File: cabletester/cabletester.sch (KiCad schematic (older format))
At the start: 25 parts, among them J1 Conn, J2 Conn, J3 Conn, J4 Conn, J5 OLED, U1 4051

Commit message: First version after fork, schematic cleanup and PCB
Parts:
- A1: footprint Module:Arduino_Nano -> ao_tht:Arduino_Nano; symbol cabletester-rescue:Arduino_Nano_v3.x-MCU_Module -> MCU_Module:Arduino_Nano_v3.x
- C1: footprint (none) -> ao_tht:C_Disc_D3.0mm_W1.6mm_P2.50mm
- J1, J3: value Conn -> IDC 2x5; footprint (none) -> ao_tht:Power_Header
- J2, J4: value Conn -> IDC 2x8; footprint (none) -> Connector_IDC:IDC-Header_2x08_P2.54mm_Vertical
- J5: footprint (none) -> Connector_PinSocket_2.54mm:PinSocket_1x04_P2.54mm_Vertical
- R1, R10, R11, R12, R13, R14, R15, R16, R17, R2, R3, R4, R5, R6, R7, R8, R9: footprint (none) -> ao_tht:R_Axial_DIN0207_L6.3mm_D2.5mm_P7.62mm_Horizontal
- U1: footprint (none) -> ao_tht:DIP-16_W7.62mm_Socket_LongPads
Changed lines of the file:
@@
 P 8900 4550
 F 0 "J4" H 8950 5067 50  0000 C CNN
-F 1 "Conn" H 8950 4976 50  0000 C CNN
-F 2 "" H 8900 4550 50  0001 C CNN
+F 1 "IDC 2x8" H 8950 4976 50  0000 C CNN
+F 2 "Connector_IDC:IDC-Header_2x08_P2.54mm_Vertical" H 8900 4550 50  0001 C CNN
 F 3 "~" H 8900 4550 50  0001 C CNN
 	1    8900 4550
@@
 P 5600 2650
 F 0 "J2" H 5650 3167 50  0000 C CNN
-F 1 "Conn" H 5650 3076 50  0000 C CNN
-F 2 "" H 5600 2650 50  0001 C CNN
+F 1 "IDC 2x8" H 5650 3076 50  0000 C CNN
+F 2 "Connector_IDC:IDC-Header_2x08_P2.54mm_Vertical" H 5600 2650 50  0001 C CNN
 F 3 "~" H 5600 2650 50  0001 C CNN
 	1    5600 2650
@@
 P 9800 4450
 F 0 "J3" H 9850 4867 50  0000 C CNN
-F 1 "Conn" H 9850 4776 50  0000 C CNN
-F 2 "" H 9800 4450 50  0001 C CNN
+F 1 "IDC 2x5" H 9850 4776 50  0000 C CNN
+F 2 "ao_tht:Power_Header" H 9800 4450 50  0001 C CNN
 F 3 "~" H 9800 4450 50  0001 C CNN
 	1    9800 4450
@@
 P 4700 2550
 F 0 "J1" H 4750 2967 50  0000 C CNN
-F 1 "Conn" H 4750 2876 50  0000 C CNN
-F 2 "" H 4700 2550 50  0001 C CNN
+F 1 "IDC 2x5" H 4750 2876 50  0000 C CNN
+F 2 "ao_tht:Power_Header" H 4700 2550 50  0001 C CNN
 F 3 "~" H 4700 2550 50  0001 C CNN
 	1    4700 2550
@@
 Connection ~ 5900 3050
 $Comp
-L cabletester-rescue:Arduino_Nano_v3.x-MCU_Module A1
+L MCU_Module:Arduino_Nano_v3.x A1
 U 1 1 5DF0BB02
 P 2300 4400
 F 0 "A1" H 2300 3100 50  0000 C CNN
 F 1 "Arduino_Nano_v3.x" H 2300 3000 50  0000 C CNN
-F 2 "Module:Arduino_Nano" H 2450 3450 50  0001 L CNN
+F 2 "ao_tht:Arduino_Nano" H 2450 3450 50  0001 L CNN
 F 3 "http://www.mouser.com/pdfdocs/Gravitech_Arduino_Nano3_0.pdf" H 2300 3400 50  0001 C CNN
 	1    2300 4400
@@
 F 0 "U1" H 5291 4304 50  0000 L CNN
 F 1 "4051" H 5291 4395 50  0000 L CNN
-F 2 "" H 4750 4350 50  0001 C CNN
+F 2 "ao_tht:DIP-16_W7.62mm_Socket_LongPads" H 4750 4350 50  0001 C CNN
 F 3 "http://www.intersil.com/content/dam/Intersil/documents/cd40/cd4051bms-52bms-53bms.pdf" H 4750 4350 50  0001 C CNN
 	1    4750 4350
@@
 F 0 "R10" H 5370 5796 50  0000 L CNN
 F 1 "10K" H 5370 5705 50  0000 L CNN
-F 2 "" V 5230 5750 50  0001 C CNN
+F 2 "ao_tht:R_Axial_DIN0207_L6.3mm_D2.5mm_P7.62mm_Horizontal" V 5230 5750 50  0001 C CNN
 F 3 "~" H 5300 5750 50  0001 C CNN
 	1    5300 5750
@@
 F 0 "R11" H 5670 5796 50  0000 L CNN
 F 1 "10K" H 5670 5705 50  0000 L CNN
-F 2 "" V 5530 5750 50  0001 C CNN
+F 2 "ao_tht:R_Axial_DIN0207_L6.3mm_D2.5mm_P7.62mm_Horizontal" V 5530 5750 50  0001 C CNN
 F 3 "~" H 5600 5750 50  0001 C CNN
 	1    5600 5750
@@
 F 0 "R12" H 5970 5796 50  0000 L CNN
 F 1 "10K" H 5970 5705 50  0000 L CNN
-F 2 "" V 5830 5750 50  0001 C CNN
+F 2 "ao_tht:R_Axial_DIN0207_L6.3mm_D2.5mm_P7.62mm_Horizontal" V 5830 5750 50  0001 C CNN
 F 3 "~" H 5900 5750 50  0001 C CNN
 	1    5900 5750
@@
 F 0 "R13" H 6270 5796 50  0000 L CNN
 F 1 "10K" H 6270 5705 50  0000 L CNN
-F 2 "" V 6130 5750 50  0001 C CNN
+F 2 "ao_tht:R_Axial_DIN0207_L6.3mm_D2.5mm_P7.62mm_Horizontal" V 6130 5750 50  0001 C CNN
 F 3 "~" H 6200 5750 50  0001 C CNN
 	1    6200 5750
@@
 F 0 "R14" H 6570 5796 50  0000 L CNN
 F 1 "10K" H 6570 5705 50  0000 L CNN
-F 2 "" V 6430 5750 50  0001 C CNN
+F 2 "ao_tht:R_Axial_DIN0207_L6.3mm_D2.5mm_P7.62mm_Horizontal" V 6430 5750 50  0001 C CNN
 F 3 "~" H 6500 5750 50  0001 C CNN
 	1    6500 5750
@@
 F 0 "R15" H 6870 5796 50  0000 L CNN
 F 1 "10K" H 6870 5705 50  0000 L CNN
-F 2 "" V 6730 5750 50  0001 C CNN
+F 2 "ao_tht:R_Axial_DIN0207_L6.3mm_D2.5mm_P7.62mm_Horizontal" V 6730 5750 50  0001 C CNN
 F 3 "~" H 6800 5750 50  0001 C CNN
 	1    6800 5750
@@
 F 0 "R16" H 7170 5796 50  0000 L CNN
 F 1 "10K" H 7170 5705 50  0000 L CNN
-F 2 "" V 7030 5750 50  0001 C CNN
+F 2 "ao_tht:R_Axial_DIN0207_L6.3mm_D2.5mm_P7.62mm_Horizontal" V 7030 5750 50  0001 C CNN
 F 3 "~" H 7100 5750 50  0001 C CNN
 	1    7100 5750
@@
 F 0 "R17" H 7470 5796 50  0000 L CNN
 F 1 "10K" H 7470 5705 50  0000 L CNN
-F 2 "" V 7330 5750 50  0001 C CNN
+F 2 "ao_tht:R_Axial_DIN0207_L6.3mm_D2.5mm_P7.62mm_Horizontal" V 7330 5750 50  0001 C CNN
 F 3 "~" H 7400 5750 50  0001 C CNN
 	1    7400 5750
@@
 F 0 "R1" H 6080 2154 50  0000 R CNN
 F 1 "1K" H 6080 2245 50  0000 R CNN
-F 2 "" V 6080 2200 50  0001 C CNN
+F 2 "ao_tht:R_Axial_DIN0207_L6.3mm_D2.5mm_P7.62mm_Horizontal" V 6080 2200 50  0001 C CNN
 F 3 "~" H 6150 2200 50  0001 C CNN
 	1    6150 2200
@@
 F 0 "R2" H 6380 2254 50  0000 R CNN
 F 1 "1K" H 6380 2345 50  0000 R CNN
-F 2 "" V 6380 2300 50  0001 C CNN
+F 2 "ao_tht:R_Axial_DIN0207_L6.3mm_D2.5mm_P7.62mm_Horizontal" V 6380 2300 50  0001 C CNN
 F 3 "~" H 6450 2300 50  0001 C CNN
 	1    6450 2300
@@
 F 0 "R3" H 6680 2354 50  0000 R CNN
 F 1 "1K" H 6680 2445 50  0000 R CNN
-F 2 "" V 6680 2400 50  0001 C CNN
+F 2 "ao_tht:R_Axial_DIN0207_L6.3mm_D2.5mm_P7.62mm_Horizontal" V 6680 2400 50  0001 C CNN
 F 3 "~" H 6750 2400 50  0001 C CNN
 	1    6750 2400
@@
 F 0 "R4" H 6980 2454 50  0000 R CNN
 F 1 "1K" H 6980 2545 50  0000 R CNN
-F 2 "" V 6980 2500 50  0001 C CNN
+F 2 "ao_tht:R_Axial_DIN0207_L6.3mm_D2.5mm_P7.62mm_Horizontal" V 6980 2500 50  0001 C CNN
 F 3 "~" H 7050 2500 50  0001 C CNN
 	1    7050 2500
@@
 F 0 "R5" H 7280 2554 50  0000 R CNN
 F 1 "1K" H 7280 2645 50  0000 R CNN
-F 2 "" V 7280 2600 50  0001 C CNN
+F 2 "ao_tht:R_Axial_DIN0207_L6.3mm_D2.5mm_P7.62mm_Horizontal" V 7280 2600 50  0001 C CNN
 F 3 "~" H 7350 2600 50  0001 C CNN
 	1    7350 2600
@@
 F 0 "R6" H 7580 2654 50  0000 R CNN
 F 1 "1K" H 7580 2745 50  0000 R CNN
-F 2 "" V 7580 2700 50  0001 C CNN
+F 2 "ao_tht:R_Axial_DIN0207_L6.3mm_D2.5mm_P7.62mm_Horizontal" V 7580 2700 50  0001 C CNN
 F 3 "~" H 7650 2700 50  0001 C CNN
 	1    7650 2700
@@
 F 0 "R7" H 7880 2754 50  0000 R CNN
 F 1 "1K" H 7880 2845 50  0000 R CNN
-F 2 "" V 7880 2800 50  0001 C CNN
+F 2 "ao_tht:R_Axial_DIN0207_L6.3mm_D2.5mm_P7.62mm_Horizontal" V 7880 2800 50  0001 C CNN
 F 3 "~" H 7950 2800 50  0001 C CNN
 	1    7950 2800
@@
 F 0 "R8" H 8180 2854 50  0000 R CNN
 F 1 "1K" H 8180 2945 50  0000 R CNN
-F 2 "" V 8180 2900 50  0001 C CNN
+F 2 "ao_tht:R_Axial_DIN0207_L6.3mm_D2.5mm_P7.62mm_Horizontal" V 8180 2900 50  0001 C CNN
 F 3 "~" H 8250 2900 50  0001 C CNN
 	1    8250 2900
@@
 F 0 "R9" H 8480 2954 50  0000 R CNN
 F 1 "1K" H 8480 3045 50  0000 R CNN
-F 2 "" V 8480 3000 50  0001 C CNN
+F 2 "ao_tht:R_Axial_DIN0207_L6.3mm_D2.5mm_P7.62mm_Horizontal" V 8480 3000 50  0001 C CNN
 F 3 "~" H 8550 3000 50  0001 C CNN
 	1    8550 3000
@@
 F 0 "C1" H 4365 5596 50  0000 L CNN
 F 1 "100n" H 4365 5505 50  0000 L CNN
-F 2 "" H 4288 5400 50  0001 C CNN
+F 2 "ao_tht:C_Disc_D3.0mm_W1.6mm_P2.50mm" H 4288 5400 50  0001 C CNN
 F 3 "~" H 4250 5550 50  0001 C CNN
 	1    4250 5550
@@
 F 0 "J5" H 3100 5200 50  0000 L CNN
 F 1 "OLED" H 3050 5300 50  0000 L CNN
-F 2 "" H 3150 5600 50  0001 C CNN
+F 2 "Connector_PinSocket_2.54mm:PinSocket_1x04_P2.54mm_Vertical" H 3150 5600 50  0001 C CNN
 F 3 "~" H 3150 5600 50  0001 C CNN
 	1    3150 5600

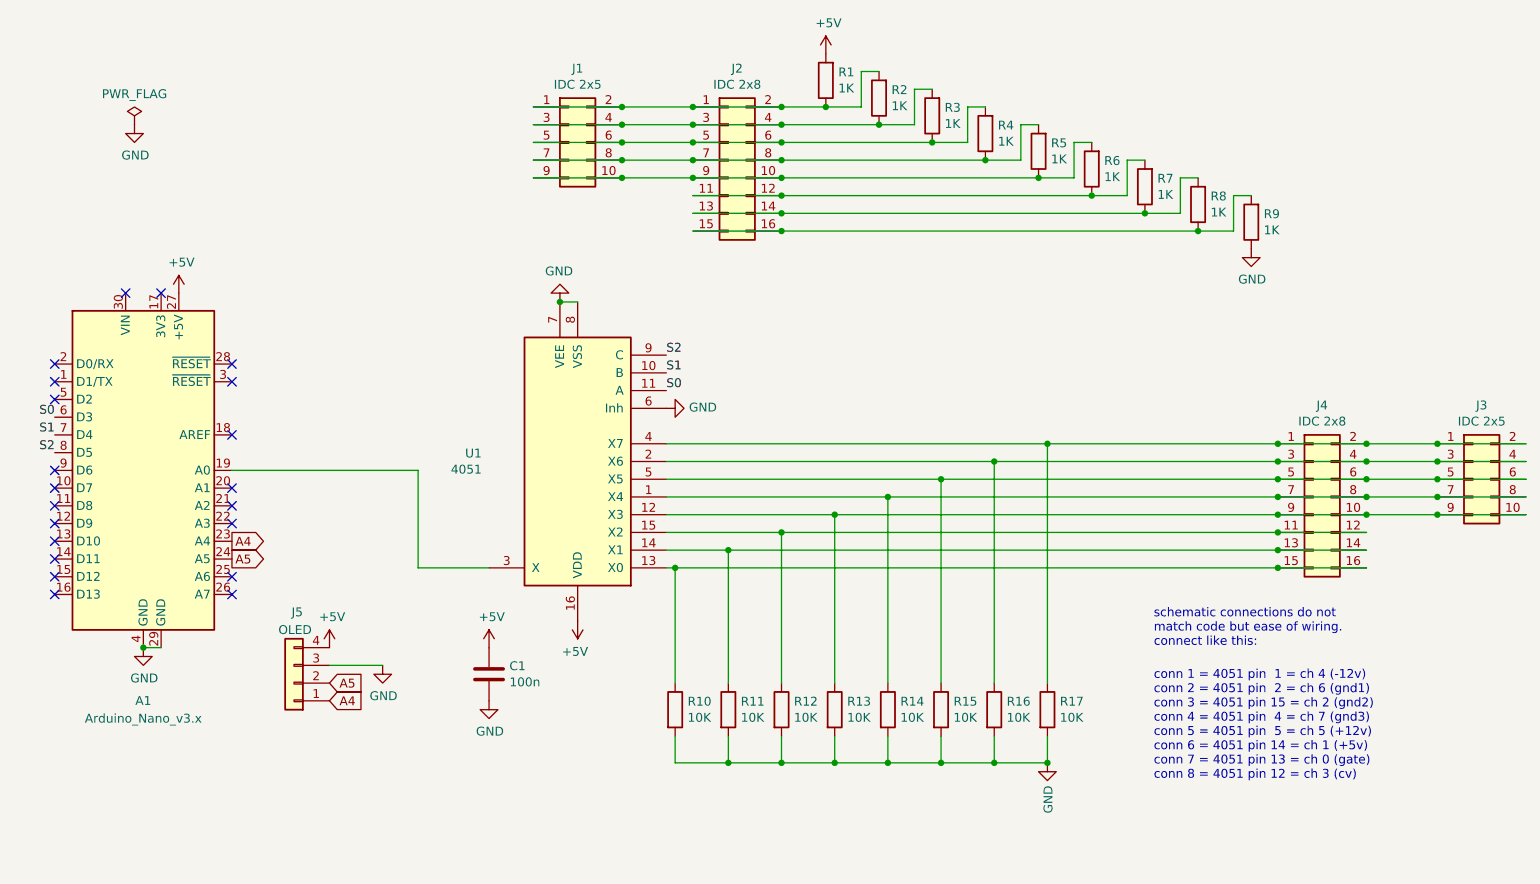
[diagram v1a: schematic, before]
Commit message: labels to globals, page settings
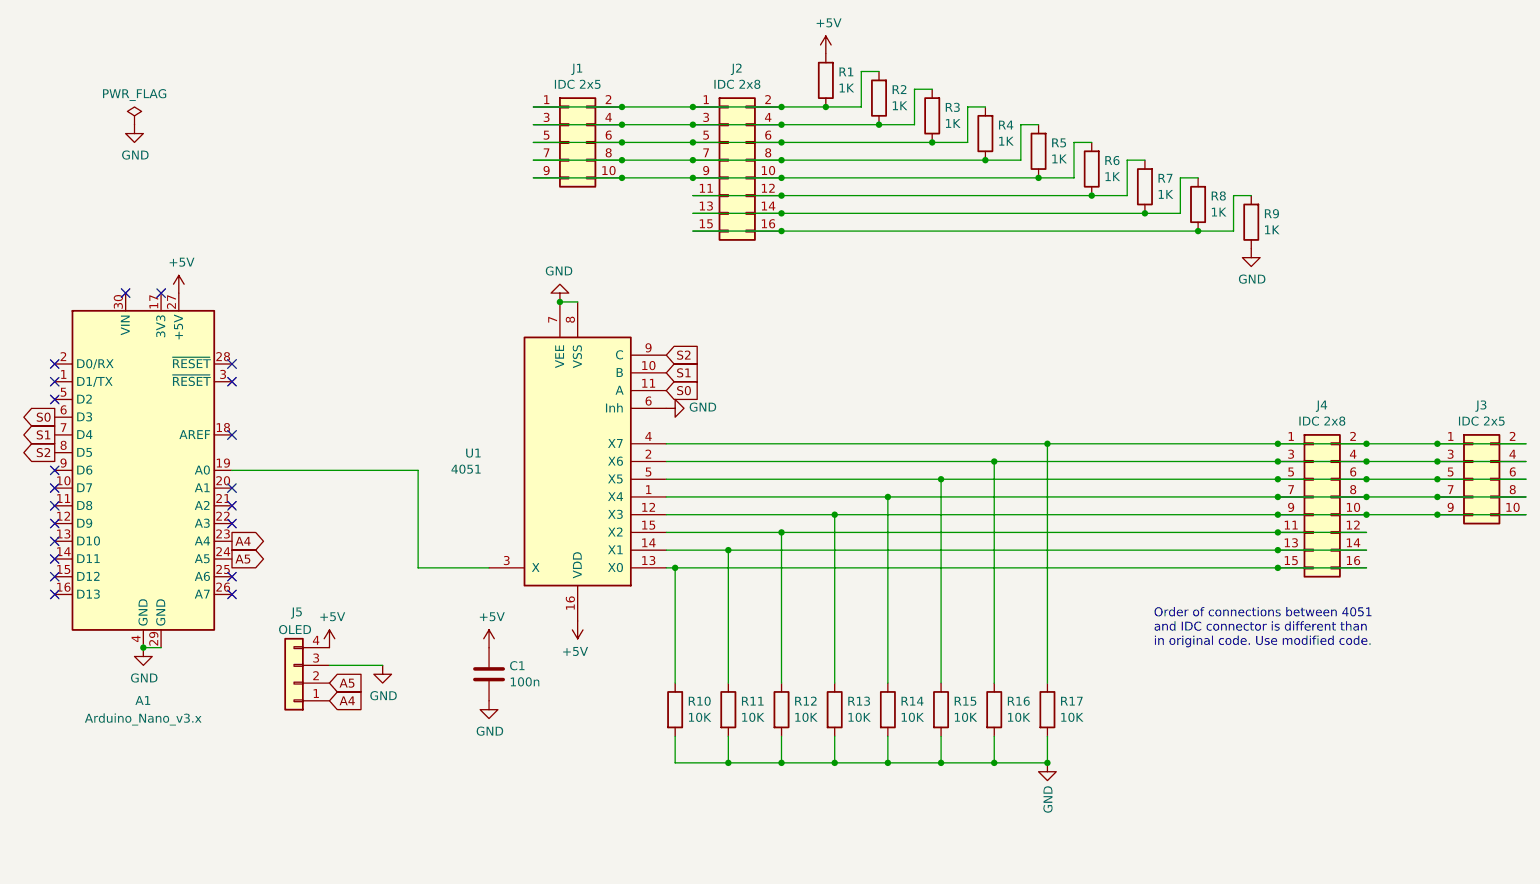
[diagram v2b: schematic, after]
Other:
- note added: "Order of connections between 4051\nand IDC connector is different than\nin original code. Use modified code."
- note removed: "conn 1 = 4051 pin 1 = ch 4 (-12v)\nconn 2 = 4051 pin 2 = ch 6 (gnd1)\nconn 3 = 4051 pin 15 = ch 2 (gnd2)\nconn 4 = 4051 pin 4 = ch 7 (gnd3)\nconn 5 = 4051 pin 5 = ch 5 (+12v)\nconn 6 = 4051 pin 14 = ch 1 (+5v)\nconn 7 = 4051 pin 13 = ch 0 (gate)\nconn 8 = 4051 pin 12 = ch 3 (cv)"
- note removed: "schematic connections do not \nmatch code but ease of wiring.\nconnect like this:"
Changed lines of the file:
@@
 Date ""
 Rev ""
-Comp ""
-Comment1 ""
+Comp "tomarus / https://github.com/tomarus/cabletester"
+Comment1 "forked to https://github.com/holmesrichards/cabletester with slight mods"
 Comment2 ""
 Comment3 ""
@@
 Connection ~ 5900 2950
 Connection ~ 5900 3050
-$Comp
-L MCU_Module:Arduino_Nano_v3.x A1
-U 1 1 5DF0BB02
-P 2300 4400
-F 0 "A1" H 2300 3100 50  0000 C CNN
-F 1 "Arduino_Nano_v3.x" H 2300 3000 50  0000 C CNN
-F 2 "ao_tht:Arduino_Nano" H 2450 3450 50  0001 L CNN
-F 3 "http://www.mouser.com/pdfdocs/Gravitech_Arduino_Nano3_0.pdf" H 2300 3400 50  0001 C CNN
-	1    2300 4400
-	1    0    0    -1
-$EndComp
 $Comp
 L power:GND #PWR011
@@
 Wire Wire Line
 	3850 4950 4250 4950
-Text Label 5250 3950 0    50   ~ 0
-S0
-Text Label 5250 3850 0    50   ~ 0
-S1
-Text Label 5250 3750 0    50   ~ 0
-S2
-Text Label 1800 4100 2    50   ~ 0
-S0
-Text Label 1800 4200 2    50   ~ 0
-S1
-Text Label 1800 4300 2    50   ~ 0
-S2
 NoConn ~ 1800 4400
 NoConn ~ 1800 4500
@@
 	1    0    0    -1
 $EndComp
-NoConn ~ 1800 4000
 NoConn ~ 1800 3900
 NoConn ~ 1800 3800
@@
 $EndComp
 Text Notes 8000 5400 0    50   ~ 0
-schematic connections do not \nmatch code but ease of wiring.\nconnect like this:
+Order of connections between 4051\nand IDC connector is different than\nin original code. Use modified code.
 Wire Wire Line
 	5300 4950 5300 5600
@@
 	1    0    0    -1
 $EndComp
-Text Notes 8000 6150 0    50   ~ 0
-conn 1 = 4051 pin  1 = ch 4 (-12v)\nconn 2 = 4051 pin  2 = ch 6 (gnd1)\nconn 3 = 4051 pin 15 = ch 2 (gnd2)\nconn 4 = 4051 pin  4 = ch 7 (gnd3)\nconn 5 = 4051 pin  5 = ch 5 (+12v)\nconn 6 = 4051 pin 14 = ch 1 (+5v)\nconn 7 = 4051 pin 13 = ch 0 (gate)\nconn 8 = 4051 pin 12 = ch 3 (cv)
 Connection ~ 6450 2450
 Wire Wire Line
@@
 	4750 3450 4650 3450
 Connection ~ 4650 3450
+NoConn ~ 1800 4000
+$Comp
+L MCU_Module:Arduino_Nano_v3.x A1
+U 1 1 5DF0BB02
+P 2300 4400
+F 0 "A1" H 2300 3100 50  0000 C CNN
+F 1 "Arduino_Nano_v3.x" H 2300 3000 50  0000 C CNN
+F 2 "ao_tht:Arduino_Nano" H 2450 3450 50  0001 L CNN
+F 3 "http://www.mouser.com/pdfdocs/Gravitech_Arduino_Nano3_0.pdf" H 2300 3400 50  0001 C CNN
+	1    2300 4400
+	1    0    0    -1
+$EndComp
+Text GLabel 1800 4100 0    50   Output ~ 0
+S0
+Text GLabel 1800 4200 0    50   Output ~ 0
+S1
+Text GLabel 1800 4300 0    50   Output ~ 0
+S2
+Text GLabel 5250 3950 2    50   Input ~ 0
+S0
+Text GLabel 5250 3850 2    50   Input ~ 0
+S1
+Text GLabel 5250 3750 2    50   Input ~ 0
+S2
 $EndSCHEMATC

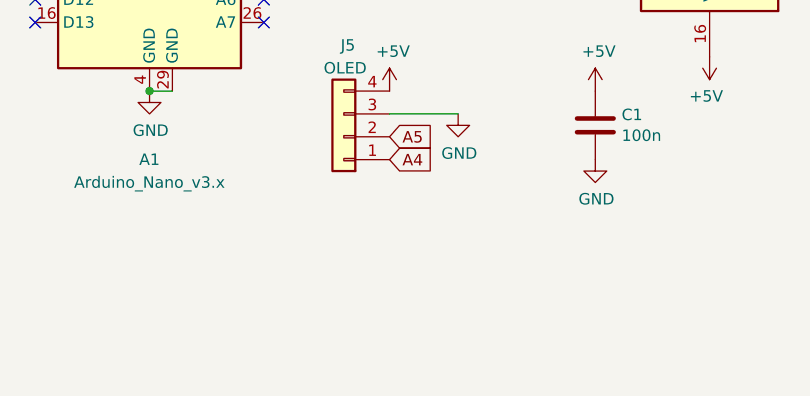
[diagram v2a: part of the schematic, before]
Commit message: Add 2nd header for alternate OLED pinout
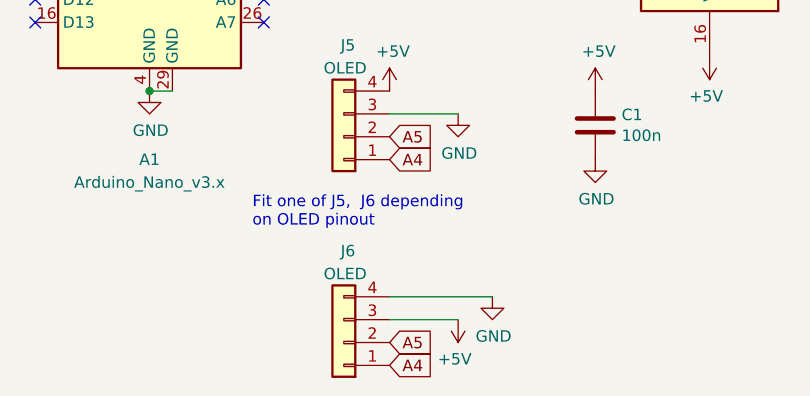
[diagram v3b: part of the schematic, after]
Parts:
- added J6: OLED, Connector_PinSocket_2.54mm:PinSocket_1x04_P2.54mm_Vertical, symbol Connector_Generic:Conn_01x04
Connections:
- net +5V: now also J6.3 (Pin_3)
- net A4: now also J6.1 (Pin_1)
- net A5: now also J6.2 (Pin_2)
- net GND: now also J6.4 (Pin_4)
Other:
- note added: "Fit one of J5, J6 depending\non OLED pinout"
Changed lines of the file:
@@
 Text GLabel 5250 3750 2    50   Input ~ 0
 S2
+$Comp
+L power:GND #PWR06
+U 1 1 5F324521
+P 3800 6300
+F 0 "#PWR06" H 3800 6050 50  0001 C CNN
+F 1 "GND" H 3805 6127 50  0000 C CNN
+F 2 "" H 3800 6300 50  0001 C CNN
+F 3 "" H 3800 6300 50  0001 C CNN
+	1    3800 6300
+	1    0    0    -1
+$EndComp
+Text GLabel 3350 6600 2    50   Input ~ 0
+A4
+Text GLabel 3350 6500 2    50   Input ~ 0
+A5
+$Comp
+L Connector_Generic:Conn_01x04 J6
+U 1 1 5F324527
+P 3150 6500
+F 0 "J6" H 3100 6100 50  0000 L CNN
+F 1 "OLED" H 3050 6200 50  0000 L CNN
+F 2 "Connector_PinSocket_2.54mm:PinSocket_1x04_P2.54mm_Vertical" H 3150 6500 50  0001 C CNN
+F 3 "~" H 3150 6500 50  0001 C CNN
+	1    3150 6500
+	-1   0    0    1
+$EndComp
+$Comp
+L power:+5V #PWR012
+U 1 1 5F32451B
+P 3650 6400
+F 0 "#PWR012" H 3650 6250 50  0001 C CNN
+F 1 "+5V" H 3665 6573 50  0000 C CNN
+F 2 "" H 3650 6400 50  0001 C CNN
+F 3 "" H 3650 6400 50  0001 C CNN
+	1    3650 6400
+	-1   0    0    1
+$EndComp
+Wire Wire Line
+	3350 6400 3650 6400
+Wire Wire Line
+	3350 6300 3800 6300
+Text Notes 2750 6000 0    50   ~ 0
+Fit one of J5,  J6 depending\non OLED pinout
 $EndSCHEMATC

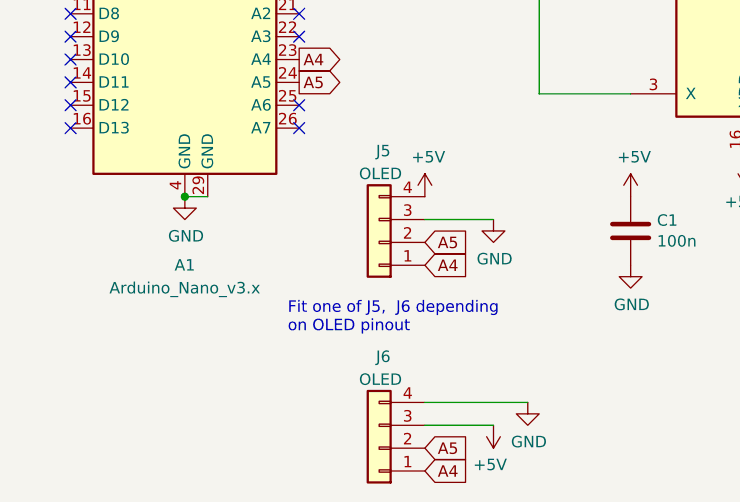
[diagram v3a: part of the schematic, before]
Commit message: BOM; change header label
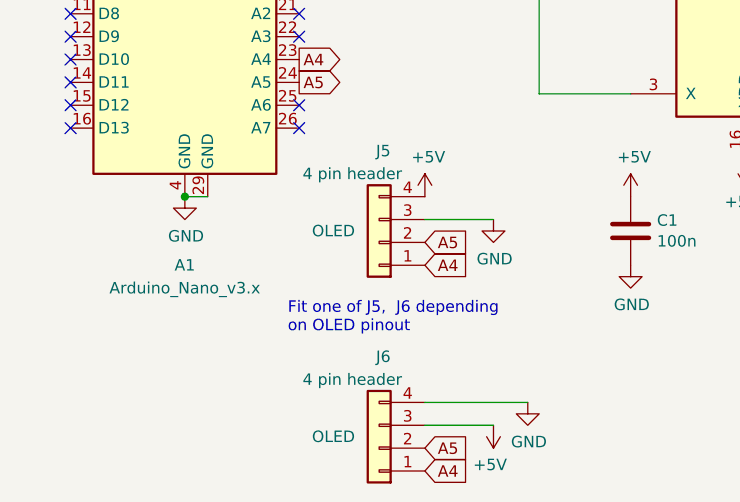
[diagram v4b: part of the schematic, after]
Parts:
- J5, J6: value OLED -> 4 pin header; Field4 (none) -> OLED
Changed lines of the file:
@@
 P 3150 5600
 F 0 "J5" H 3100 5200 50  0000 L CNN
-F 1 "OLED" H 3050 5300 50  0000 L CNN
+F 1 "4 pin header" H 3050 5300 50  0000 L CNN
 F 2 "Connector_PinSocket_2.54mm:PinSocket_1x04_P2.54mm_Vertical" H 3150 5600 50  0001 C CNN
 F 3 "~" H 3150 5600 50  0001 C CNN
+F 4 "OLED" H 3350 5550 50  0000 C CNN "Field4"
 	1    3150 5600
 	-1   0    0    1
@@
 P 3150 6500
 F 0 "J6" H 3100 6100 50  0000 L CNN
-F 1 "OLED" H 3050 6200 50  0000 L CNN
+F 1 "4 pin header" H 3050 6200 50  0000 L CNN
 F 2 "Connector_PinSocket_2.54mm:PinSocket_1x04_P2.54mm_Vertical" H 3150 6500 50  0001 C CNN
 F 3 "~" H 3150 6500 50  0001 C CNN
+F 4 "OLED" H 3350 6450 50  0000 C CNN "Field4"
 	1    3150 6500
 	-1   0    0    1
